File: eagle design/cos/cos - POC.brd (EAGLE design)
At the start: 35 x 63 mm, 97 parts, among them IC1 TPS630702RNMT, IC10 LM74670QDGKRQ1, IC11 SQJ886EP-T1_GE3, IC13 LDK320M50R, IC14 MCP2515, IC15 LM74670QDGKRQ1, IC16 MCP2561-2, IC17 AD5160BRJZ5-R2, IC18 MP3221GJ-P, IC2 LM74670QDGKRQ1, IC3 LMP92064SD/NOPB, IC4 SQJ960EP-T1_GE3, IC5 ATTINY4313-MMH, IC6 LM74670QDGKRQ1, IC7 PBRC8.00GR50X000, IC8 LM74670QDGKRQ1, IC9 SQJ960EP-T1_GE3, J1 22-27-2021-02

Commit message: - added MCP23S08 - 8-Bit IO Expander with Serial Interface
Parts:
- removed JP4: (no value), jumper:JP1
- added C35: 22μF, rcl:C0402
- added IC19: MP3221GJ-P, MP3221–2.7A, 1.2MHZ, HIGH-EFFICIENCY STEP UP CONVERTER WITH INPUT DISCONNECT:TSOT23-6
- added R23: 120, rcl:R0402
- added TP8: PTR1TP10SQ, testpad:TP10SQ
- C27: value 1μF -> 0.1μF
- C29: value 4.7μF -> 1μF
- C30: value 0.1μF -> 4.7μF
- C32: value 10μF -> 0.1μF
- C33: value 0.1μF -> 10μF
- C34: value 22μF -> 0.1μF
- IC15: value LM74670QDGKRQ1 -> MCP23S08-E/ML; device LM74670 - Smart Diode Rectifier Controller:VSSOP-8 -> MCP23S08 - 8-Bit IO Expander with Serial Interface:QFN20
- IC16: value MCP2561-2 -> LM74670QDGKRQ1; device MCP2561-2 - High-Speed CAN Transceiver:DFN10 -> LM74670 - Smart Diode Rectifier Controller:VSSOP-8
- IC17: value AD5160BRJZ5-R2 -> MCP2561-2; device ad5160 - 256-Position SPI-Compatible Digital Potentiometer:SOT-23-8 -> MCP2561-2 - High-Speed CAN Transceiver:DFN10
- IC18: value MP3221GJ-P -> AD5160BRJZ5-R2; device MP3221–2.7A, 1.2MHZ, HIGH-EFFICIENCY STEP UP CONVERTER WITH INPUT DISCONNECT:TSOT23-6 -> ad5160 - 256-Position SPI-Compatible Digital Potentiometer:SOT-23-8
- R12: value 741X083103JP / 10kΩ -> 1k; device 741X083331JP Resistor Array:0402 -> rcl:R0402
- R13: value 1k -> 270k
- R14: value 270k -> 741X083331JP / 330Ω; device rcl:R0402 -> 741X083331JP Resistor Array:0402
- R15: value thermistor NTC 10k -> 741X083103JP / 10kΩ; device rcl:V526-0 -> 741X083331JP Resistor Array:0402
- R16: value 741X083331JP / 330Ω -> 10k; device 741X083331JP Resistor Array:0402 -> rcl:R0402
- R17: value 22k -> thermistor NTC 10k; device rcl:R0402 -> rcl:V526-0
- R18: value 100k -> 22k
- R20: value 653k -> 100k
- R21: value 100k -> 653k
- R22: value 120 -> 100k
- TP6: value PTR1TP10SQ -> Li-Ion Cell +; device testpad:TP10SQ -> testpad:P1-13
- moved R16 183.8 mm to (3.00, -79.5), flipped to the top, turned to 0 degrees
- moved TP5 181.0 mm to (170.0, 18.0)
- moved C26 177.2 mm to (3.50, -74.5), flipped to the top, turned to 0 degrees
- moved JP1 109.9 mm to (101.5, 42.5), turned to 180 degrees
- moved R19 77.3 mm to (102.0, 48.2), turned to 0 degrees
- moved TP6 73.9 mm to (170.0, 20.5)
- moved R17 67.3 mm to (166.8, 31.2), turned to 0 degrees
- moved C30 63.6 mm to (169.8, 29.5), turned to 270 degrees
- moved C31 55.7 mm to (110.2, 52.0), turned to 180 degrees
- moved IC16 55.2 mm to (110.2, 52.0), flipped to the top
- moved IC15 55.0 mm to (162.0, 33.5), turned to 90 degrees
- moved C32 17.9 mm to (154.0, 17.5), turned to 90 degrees
- moved R15 16.1 mm to (154.5, 20.8), turned to 90 degrees
- moved IC17 15.3 mm to (151.2, 15.0), flipped to the bottom, turned to 270 degrees
- moved C29 14.7 mm to (159.8, 18.8), turned to 0 degrees
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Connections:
- net INT renamed INT_MCP2515
- removed net SPI_SS: IC14.!CS!, IC5.14, R16.7
- new net 5V9_LDO: IC15.4_!RESET!
- new net INT_MCP23S08: IC15.7_INT
- new net MCP23S08_GP0: IC15.9_GP0
- new net MCP23S08_GP1: IC15.10_GP1
- new net MCP23S08_GP2: IC15.11_GP2
- new net MCP23S08_GP3: IC15.12_GP3
- new net MCP23S08_GP4: IC15.13_GP4
- new net MCP23S08_GP5: IC15.14_GP5
- new net MCP23S08_GP6: IC15.15_GP6
- new net MCP23S08_GP7: IC15.16_GP7
- new net SPI_SS_MCP23S08: IC15.5_!CS!, R16.1
- new net SPI_SS_MCP2515: IC14.!CS!, IC5.14, R14.7
- net 5V0_LDO: now also C27.1, C29.2, C32.1, IC15.18_VCC, IC17.VDD, R14.8, R15.1, R15.3, R15.5, R15.7, R16.2; no longer C28.2, C31.1, IC16.VDD, R12.1, R12.3, R12.5, R12.7, R16.8
- net 5V0_TP-OUT: now also C34.1, IC18.2_VDD; no longer C33.1, IC17.2_VDD
- net 6V0: now also C28.1, C35.1, R21.2; no longer C27.1, C34.1, R20.2
- net AD5160_CS: now also IC18.6_!CS!, R15.8; no longer IC17.6_!CS!, R12.8
- net CANH: now also IC17.CANH, R23.2; no longer IC16.CANH, R22.2
- net CANL: now also IC17.CANL, R23.1; no longer IC16.CANL, R22.1
- net COMP_IN: now also R19.2; no longer R18.2
- net D4_GATE: now also IC16.GATE_DRIVE, IC16.GATE_PULLD; no longer IC15.GATE_DRIVE, IC15.GATE_PULLD
- net D4_VCAPH: now also C31.2, IC16.VCAPH; no longer C30.2, IC15.VCAPH
- net D4_VCAPL: now also C31.1, IC16.VCAPL; no longer C30.1, IC15.VCAPL
- net DELON_1: now also JP3.1; no longer JP4.1
- net DYNAMO2_C: now also JP2.2; no longer JP3.2
- net DYNAMO_2: now also IC16.CATHODE, JP1.1, JP3.2; no longer IC15.CATHODE, JP3.1, JP4.2
- net EN: now also IC19.4_EN, R20.1; no longer IC18.4_EN, R19.1
- net FB: now also IC19.3_FB, R21.1, R22.2; no longer IC18.3_FB, R20.1, R21.2
- net GND: now also C28.2, C30.1, C35.2, IC15.17_GND, IC15.2_A1, IC15.3_A0, IC15.GND, IC16.ANODE, IC17.GND, IC17.VSS, IC18.3_GND, IC18.7_B, IC19.2_GND, R13.1, R18.1, R22.1, TP5.TP; no longer C28.1, C31.2, IC15.ANODE, IC16.GND, IC16.VSS, IC17.3_GND, IC17.7_B, IC18.2_GND, R14.1, R15.1, R21.1
- net ICSP_DI/MISO: now also R14.5; no longer R16.5
- net ICSP_DO/MOSI: now also R14.3; no longer R16.3
- net ICSP_SCK: now also R14.1; no longer R16.1
- net LMP92064SD_CS: now also R15.6; no longer R12.6
- net N$2: now also JP1.2; no longer JP2.2
- net N$4: now also R18.2, R19.1; no longer R17.2, R18.1
- net N$8: now also R12.2, R17.2; no longer R14.2, R15.2
- net PROG1: now also IC18.1_W; no longer IC17.1_W
- net RESET: now also R15.4; no longer R12.4
- net RXCAN: now also IC17.RXD; no longer IC16.RXD
- net SPI_MISO: now also IC15.20_MISO, R14.6; no longer R16.6
- net SPI_MOSI: now also IC15.1_MOSI, IC18.5_SDI, R14.4; no longer IC17.5_SDI, R16.4
- net SPI_SCK: now also IC15.19_SCK, IC18.4_CLK, R14.2; no longer IC17.4_CLK, R16.2
- net STBY: now also IC17.STBY, R15.2; no longer IC16.STBY, R12.2
- net SW: now also IC19.1_SW; no longer IC18.1_SW
- net THERM: now also R12.1; no longer R13.1
- net TXCAN: now also IC17.TXD; no longer IC16.TXD
- net V_LI-ION_BATTERY: now also TP6.TP; no longer TP5.TP
- net V_LI-ION_OUT: now also C30.2, C33.1, IC19.5_IN, R20.2; no longer C29.2, C32.1, IC18.5_IN, R19.2
- net V_REGULATED_TP-IN: now also TP7.TP; no longer TP6.TP
- net V_REGULATED_TP-OUT: now also TP8.TP; no longer TP7.TP
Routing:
- net SPI_SS_MCP2515: track 0.00 -> 11.4 mm, vias 0 -> 1
- net SPI_SS: track 11.4 -> 0.00 mm, vias 1 -> 0
- net V_LI-ION_BATTERY: track 4.74 -> 7.71 mm

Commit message: - added FDMQ8403 4x N-Channel quad FET for FET-based bridge rectifier - added SQJ952EP-T1_GE3 - Dual N-Fet for FET-based AC capacitor switch
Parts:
- added IC20, IC21, IC22: SQJ952EP-T1_GE3, SQJ952EP-T1_GE3 - Dual N-Fet:SO-8L
- added IC23: (no value), FDMQ8403 4x N-Channel Fet:MLP-12
- added R24, R25, R26: 10k, rcl:R0402
- moved R16 198.9 mm to (167.0, 33.0), turned to 180 degrees
- moved C26 189.0 mm to (157.0, 35.8)
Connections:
- removed net N$2: C5.-, JP1.2
- new net GATE_DELON: IC22.G1, IC22.G2, R24.2
- new net GATE_GRAETZ: IC21.G1, IC21.G2, R25.1
- new net GATE_TUNING-CAP: IC20.G1, IC20.G2, R26.2
- new net N$13: IC20.S1, IC20.S2
- new net N$16: IC21.S1, IC21.S2
- new net N$20: IC22.S1, IC22.S2
- new net TUNING_CAP_DRAIN: C5.-, IC20.D1_1, IC20.D1_2, IC20.D1_3, JP1.2
- net 5V0_LDO: now also R25.2
- net DELON_1: now also IC22.D1_1, IC22.D1_2, IC22.D1_3
- net DYNAMO2_C: now also IC21.D1_1, IC21.D1_2, IC21.D1_3
- net DYNAMO_2: now also IC20.D2_1, IC20.D2_2, IC20.D2_3, IC21.D2_1, IC21.D2_2, IC21.D2_3, IC22.D2_1, IC22.D2_2, IC22.D2_3
- net GND: now also R24.1, R26.1
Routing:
- net TUNING_CAP_DRAIN: track 0.00 -> 9.91 mm
- net N$2: track 9.91 -> 0.00 mm
- net N$20: track 0.00 -> 4.44 mm
- net N$16: track 0.00 -> 4.44 mm
- net N$13: track 0.00 -> 4.44 mm
- net GATE_TUNING-CAP: track 0.00 -> 4.14 mm
- net GATE_GRAETZ: track 0.00 -> 4.14 mm
- net GATE_DELON: track 0.00 -> 4.14 mm

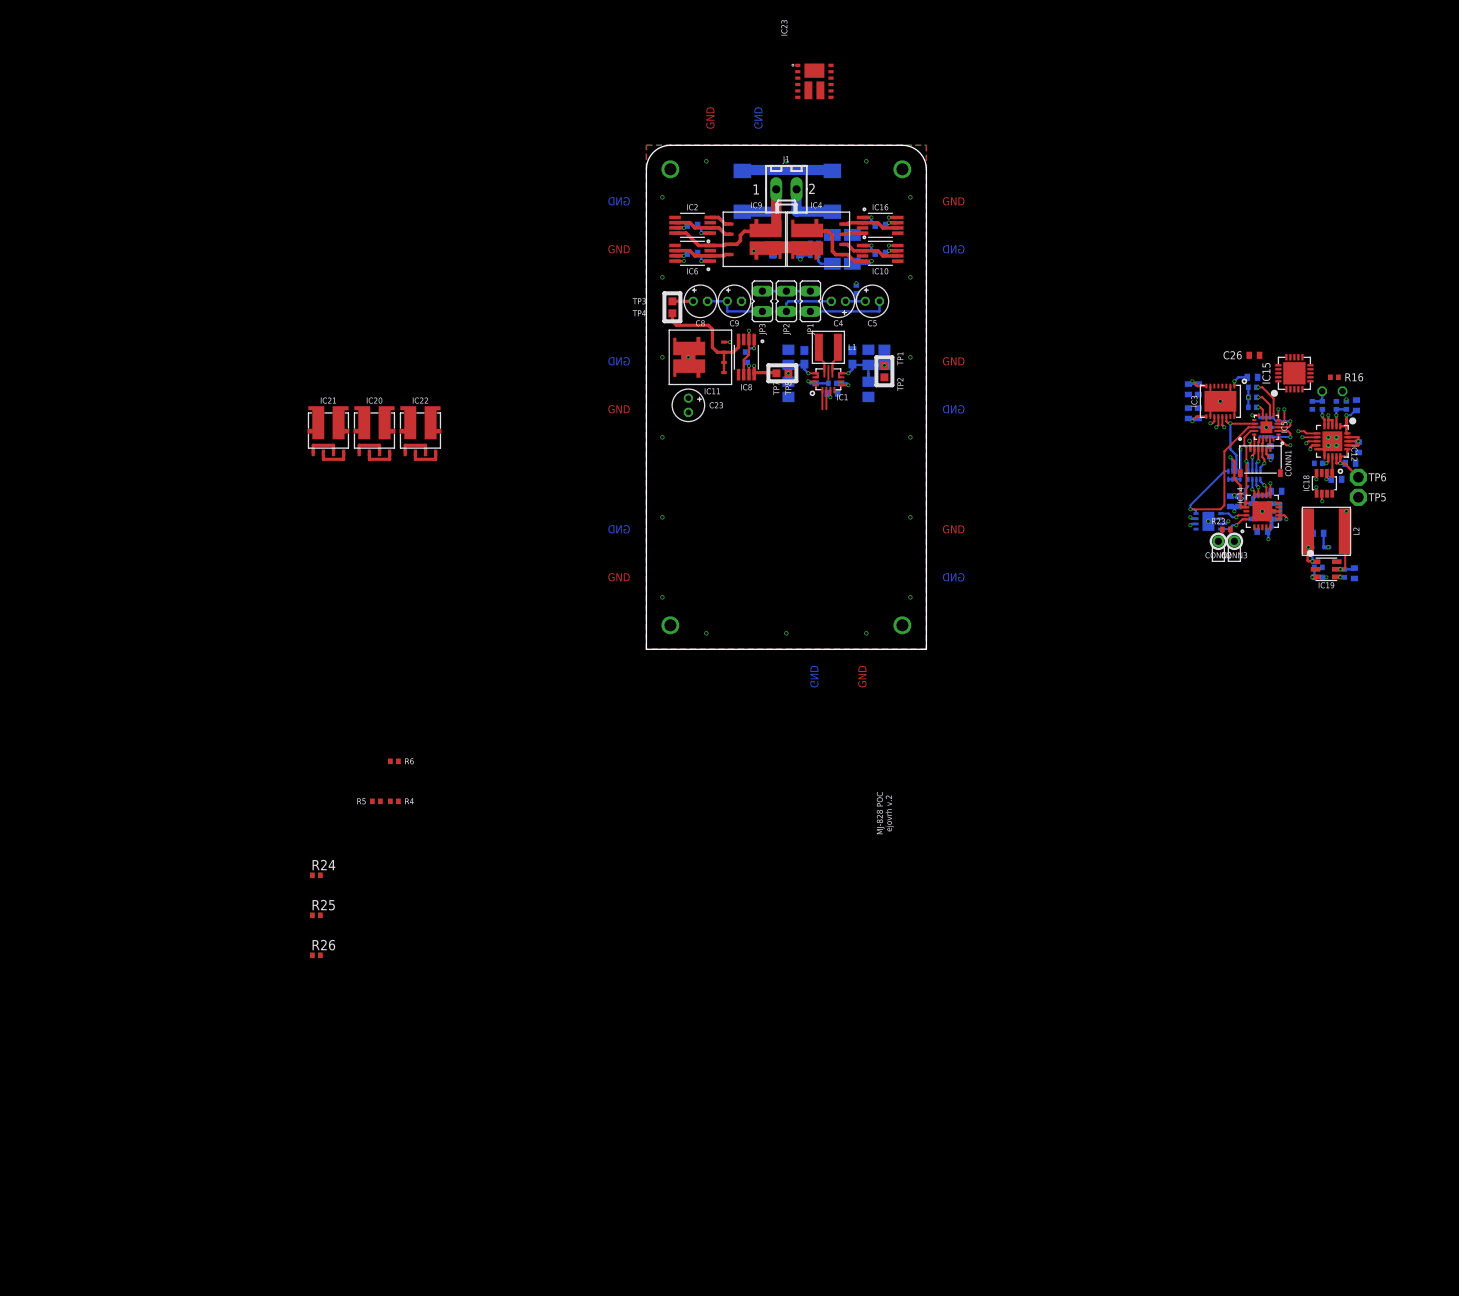
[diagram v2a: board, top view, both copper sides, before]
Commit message: - work on cos: replaced 2 fet bridge with one quad fet: FDMQ8403 4x N-Channel Fet
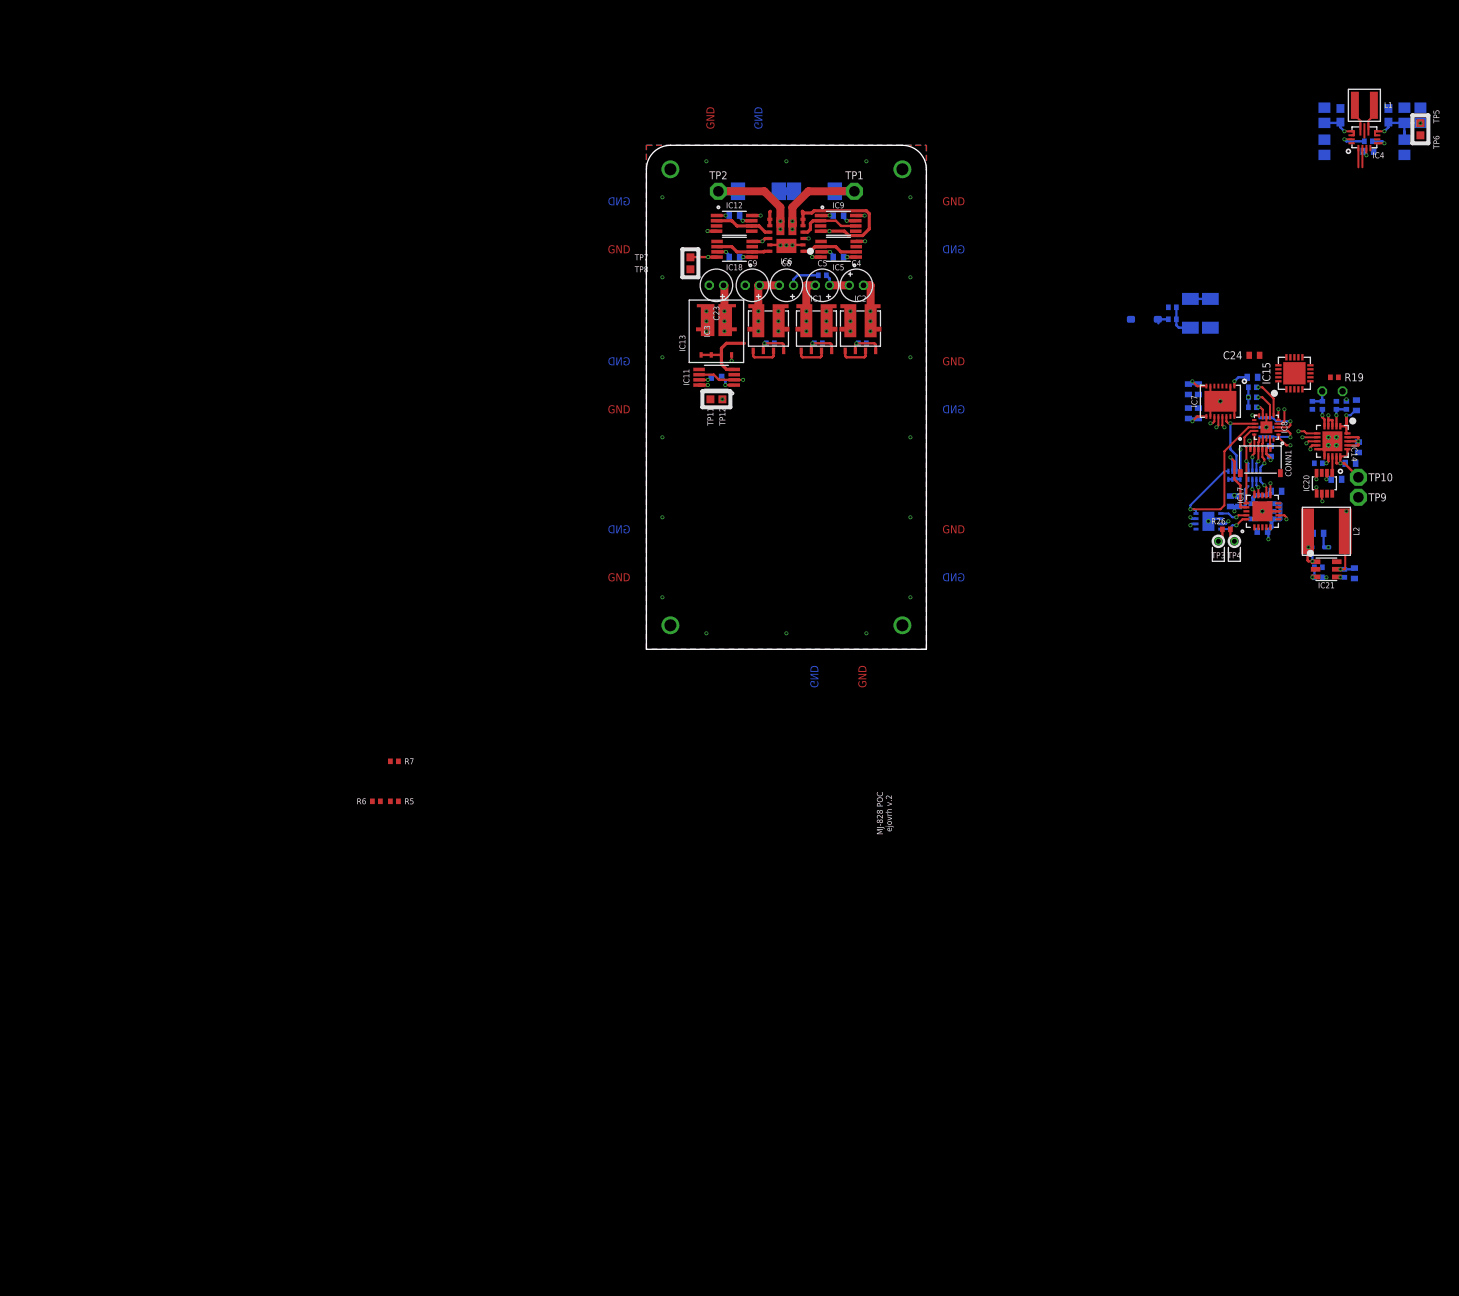
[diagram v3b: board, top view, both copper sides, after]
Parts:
- removed CONN2: CAN Low, signal testpoint:TH-0.9MM
- removed CONN3: CAN High, signal testpoint:TH-0.9MM
- removed IC22: SQJ952EP-T1_GE3, SQJ952EP-T1_GE3 - Dual N-Fet:SO-8L
- removed IC23: (no value), FDMQ8403 4x N-Channel Fet:MLP-12
- removed J1: 22-27-2021-02, con-molex:6410-02
- removed JP1, JP2, JP3: (no value), jumper:JP1
- added TP10, TP9: Li-Ion Cell +, testpad:P1-13
- added TP11, TP12: PTR1TP10SQ, testpad:TP10SQ
- C12: value 10μF -> 1μF; device rcl:C0805 -> rcl:C0402
- C14: value 1μF -> 10pF
- C18: value 10pF -> 10μF; device rcl:C0402 -> rcl:C0805
- C24: value 10μF -> 0.1μF
- C25: value 0.1μF -> 10μF
- IC1: value TPS630702RNMT -> SQJ952EP-T1_GE3; device TPS630701 - Buck Boost 5V regulator:VQFN -> SQJ952EP-T1_GE3 - Dual N-Fet:SO-8L
- IC10: value LM74670QDGKRQ1 -> PBRC8.00GR50X000; device LM74670 - Smart Diode Rectifier Controller:VSSOP-8 -> PRQV8.00CR1510Y00L - 8MHz resonator:SMT
- IC11: value SQJ886EP-T1_GE3 -> LM74670QDGKRQ1; device SQJ886EP - N-FET:SO-8L -> LM74670 - Smart Diode Rectifier Controller:VSSOP-8
- IC12: value (none) -> LM74670QDGKRQ1; device MCP73871 - Powerpath and Charge Controller:QFN50P400X400X100-21N -> LM74670 - Smart Diode Rectifier Controller:VSSOP-8
- IC13: value LDK320M50R -> SQJ886EP-T1_GE3; device LDK320 5V LDO:SOT-23-5L -> SQJ886EP - N-FET:SO-8L
- IC14: value MCP2515 -> (none); device MCP2515-I-ML - Standalonce CAN Controller with SPI Interface:QFN20 -> MCP73871 - Powerpath and Charge Controller:QFN50P400X400X100-21N
- IC16: value LM74670QDGKRQ1 -> LDK320M50R; device LM74670 - Smart Diode Rectifier Controller:VSSOP-8 -> LDK320 5V LDO:SOT-23-5L
- IC17: value MCP2561-2 -> MCP2515; device MCP2561-2 - High-Speed CAN Transceiver:DFN10 -> MCP2515-I-ML - Standalonce CAN Controller with SPI Interface:QFN20
- IC18: value AD5160BRJZ5-R2 -> LM74670QDGKRQ1; device ad5160 - 256-Position SPI-Compatible Digital Potentiometer:SOT-23-8 -> LM74670 - Smart Diode Rectifier Controller:VSSOP-8
- IC19: value MP3221GJ-P -> MCP2561-2; device MP3221–2.7A, 1.2MHZ, HIGH-EFFICIENCY STEP UP CONVERTER WITH INPUT DISCONNECT:TSOT23-6 -> MCP2561-2 - High-Speed CAN Transceiver:DFN10
- IC2: value LM74670QDGKRQ1 -> SQJ952EP-T1_GE3; device LM74670 - Smart Diode Rectifier Controller:VSSOP-8 -> SQJ952EP-T1_GE3 - Dual N-Fet:SO-8L
- IC20: value SQJ952EP-T1_GE3 -> AD5160BRJZ5-R2; device SQJ952EP-T1_GE3 - Dual N-Fet:SO-8L -> ad5160 - 256-Position SPI-Compatible Digital Potentiometer:SOT-23-8
- IC21: value SQJ952EP-T1_GE3 -> MP3221GJ-P; device SQJ952EP-T1_GE3 - Dual N-Fet:SO-8L -> MP3221–2.7A, 1.2MHZ, HIGH-EFFICIENCY STEP UP CONVERTER WITH INPUT DISCONNECT:TSOT23-6
- IC3: value LMP92064SD/NOPB -> SQJ952EP-T1_GE3; device LMP92064SD - LMP92064 Precision Low-Side, 125-kSps Simultaneous Sampling Current Sensor and Voltage Monitor With SPI:WS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 -> SQJ952EP-T1_GE3 - Dual N-Fet:SO-8L
- IC4: value SQJ960EP-T1_GE3 -> TPS630702RNMT; device SQJ960EP - dual N-FET:SO-8L -> TPS630701 - Buck Boost 5V regulator:VQFN
- IC5: value ATTINY4313-MMH -> LM74670QDGKRQ1; device ATtiny4313 microcontroller:VQFN-20 -> LM74670 - Smart Diode Rectifier Controller:VSSOP-8
- IC6: value LM74670QDGKRQ1 -> FDMQ8403; device LM74670 - Smart Diode Rectifier Controller:VSSOP-8 -> FDMQ8403 4x N-Channel Fet:MLP-12
- IC7: value PBRC8.00GR50X000 -> LMP92064SD/NOPB; device PRQV8.00CR1510Y00L - 8MHz resonator:SMT -> LMP92064SD - LMP92064 Precision Low-Side, 125-kSps Simultaneous Sampling Current Sensor and Voltage Monitor With SPI:WS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
- IC8: value LM74670QDGKRQ1 -> ATTINY4313-MMH; device LM74670 - Smart Diode Rectifier Controller:VSSOP-8 -> ATtiny4313 microcontroller:VQFN-20
- IC9: value SQJ960EP-T1_GE3 -> LM74670QDGKRQ1; device SQJ960EP - dual N-FET:SO-8L -> LM74670 - Smart Diode Rectifier Controller:VSSOP-8
- R1: value 47k -> 10k
- R10: value 10k -> 47k
- R11, R4: value 100k -> 47k
- R12: value 1k -> 47k
- R13: value 270k -> 10k
- R14: value 741X083331JP / 330Ω -> 100k; device 741X083331JP Resistor Array:0402 -> rcl:R0402
- R15: value 741X083103JP / 10kΩ -> 1k; device 741X083331JP Resistor Array:0402 -> rcl:R0402
- R16: value 10k -> 270k
- R17: value thermistor NTC 10k -> 741X083331JP / 330Ω; device rcl:V526-0 -> 741X083331JP Resistor Array:0402
- R18: value 22k -> 741X083103JP / 10kΩ; device rcl:R0402 -> 741X083331JP Resistor Array:0402
- R19: value 100k -> 10k
- R2: value 337k -> 10k
- R20: value 100k -> thermistor NTC 10k; device rcl:R0402 -> rcl:V526-0
- R21: value 653k -> 22k
- R23: value 120 -> 100k
- R24: value 10k -> 653k
- R25: value 10k -> 100k
- R26: value 10k -> 120
- R3: value 110k -> 10k
- R7: value 47k -> 100k
- R8: value 47k -> 337k
- R9: value 47k -> 110k
- TP1, TP2: value PTR1TP10SQ -> Li-Ion Cell +; device testpad:TP10SQ -> testpad:P1-13
- TP3: value PTR1TP10SQ -> CAN Low; device testpad:TP10SQ -> signal testpoint:TH
- TP4: value PTR1TP10SQ -> CAN High; device testpad:TP10SQ -> signal testpoint:TH
- TP5, TP6: value Li-Ion Cell + -> PTR1TP10SQ; device testpad:P1-13 -> testpad:TP10SQ
- moved R25 132.6 mm to (165.0, 9.25), flipped to the bottom
- moved R24 130.7 mm to (165.0, 8.00), flipped to the bottom, turned to 180 degrees
- moved IC21 126.0 mm to (166.0, 9.00), turned to 270 degrees
- moved R26 125.6 mm to (153.5, 14.0)
- moved IC20 119.0 mm to (165.8, 19.8), turned to 180 degrees
- moved R7 116.0 mm to (49.5, -15.0), flipped to the top
- moved R4 84.8 mm to (103.0, 45.8), flipped to the bottom
- moved IC12 79.6 mm to (92.0, 52.2)
- moved IC18 79.3 mm to (92.0, 49.0), turned to 90 degrees
- moved IC4 77.3 mm to (170.8, 63.0), turned to 90 degrees
- moved C13 77.0 mm to (177.8, 65.8), turned to 90 degrees
- moved TP4 75.8 mm to (154.5, 12.5), turned to 180 degrees
- moved TP3 74.6 mm to (152.5, 12.5), turned to 180 degrees
- moved C1 73.5 mm to (165.8, 61.8)
- moved C10 73.5 mm to (173.8, 65.8)
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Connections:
- removed net D1_GATE: IC2.GATE_DRIVE, IC2.GATE_PULLD, IC4.G1
- removed net D2_GATE: IC4.G2, IC6.GATE_DRIVE, IC6.GATE_PULLD
- removed net D3_GATE: IC10.GATE_DRIVE, IC10.GATE_PULLD, IC9.G1
- removed net D4_GATE: IC16.GATE_DRIVE, IC16.GATE_PULLD, IC9.G2
- removed net DYNAMO2_C: C4.-, IC21.D1_1, IC21.D1_2, IC21.D1_3, JP2.2
- new net GATE_D1: IC5.GATE_DRIVE, IC5.GATE_PULLD, IC6.1_G1
- new net GATE_D2: IC6.4_G2, IC9.GATE_DRIVE, IC9.GATE_PULLD
- new net GATE_D3: IC12.GATE_DRIVE, IC12.GATE_PULLD, IC6.9_G3
- new net GATE_D4: IC18.GATE_DRIVE, IC18.GATE_PULLD, IC6.12_G4
- net 5V0_LDO: now also C19.1, C24.1, IC16.OUT, IC19.VDD, IC8.18, R17.8, R18.1, R18.3, R18.5, R18.7, R19.2, R2.2; no longer C15.1, C26.1, IC13.OUT, IC14.VDD, IC5.18, R14.8, R15.1, R15.3, R15.5, R15.7, R16.2, R25.2
- net 5V0_TP-IN: now also C18.1, IC4.5-FB, IC4.7-VOUT, IC4.8-VOUT, IC4.VOUT, R13.2, TP5.TP; no longer C12.1, IC1.5-FB, IC1.7-VOUT, IC1.8-VOUT, IC1.VOUT, R10.2, TP1.TP
- net 5V0_TP-OUT: now also C14.1, C15.1, C25.1, IC14.17_CE, IC14.18_IN1, IC14.19_IN2, IC14.3_SEL, IC14.4_PROG2, IC14.9_!TE!, IC20.2_VDD, IC7.8_VDD, IC7.9_VDIG, R10.2, R11.2, R12.2, TP6.TP; no longer C18.1, C19.1, C24.1, IC12.17_CE, IC12.18_IN1, IC12.19_IN2, IC12.3_SEL, IC12.4_PROG2, IC12.9_!TE!, IC18.2_VDD, IC3.8_VDD, IC3.9_VDIG, R2.2, R7.2, R9.2, TP2.TP
- net 6V0: now also IC16.EN, IC16.IN, R24.2; no longer IC13.EN, IC13.IN, R21.2
- net AD5160_CS: now also IC20.6_!CS!, IC8.1, R18.8; no longer IC18.6_!CS!, IC5.1, R15.8
- net CANH: now also IC19.CANH, R26.2, TP4.TP$1; no longer CONN3.TP$1, IC17.CANH, R23.2
- net CANL: now also IC19.CANL, R26.1, TP3.TP$1; no longer CONN2.TP$1, IC17.CANL, R23.1
- net CLOCKOUT: now also IC17.OSC1, IC8.4; no longer IC14.OSC1, IC5.4
- net COMP_IN: now also IC8.10, R22.2; no longer IC5.10, R19.2
- net D1_VCAPH: now also IC5.VCAPH; no longer IC2.VCAPH
- net D1_VCAPL: now also IC5.VCAPL; no longer IC2.VCAPL
- net D2_VCAPH: now also IC9.VCAPH; no longer IC6.VCAPH
- net D2_VCAPL: now also IC9.VCAPL; no longer IC6.VCAPL
- net D3_VCAPH: now also C26.2, IC12.VCAPH; no longer C25.2, IC10.VCAPH
- net D3_VCAPL: now also C26.1, IC12.VCAPL; no longer C25.1, IC10.VCAPL
- net D4_VCAPH: now also IC18.VCAPH; no longer IC16.VCAPH
- net D4_VCAPL: now also IC18.VCAPL; no longer IC16.VCAPL
- net D5_VCAPH: now also IC11.VCAPH; no longer IC8.VCAPH
- net D5_VCAPL: now also IC11.VCAPL; no longer IC8.VCAPL
- net DEBUGWIRE/RESET: now also IC8.19; no longer IC5.19
- net DELON_1: now also IC3.D1_1, IC3.D1_2, IC3.D1_3; no longer IC22.D1_1, IC22.D1_2, IC22.D1_3, JP3.1
- net DYNAMO_1: now also IC12.CATHODE, IC18.ANODE, IC6.10_D3/S4, IC6.D3/S4, TP2.TP; no longer IC2.CATHODE, IC4.D1, IC4.S2, IC6.ANODE, J1.1
- net DYNAMO_2: now also IC1.D2_1, IC1.D2_2, IC1.D2_3, IC2.D1_1, IC2.D1_2, IC2.D1_3, IC3.D2_1, IC3.D2_2, IC3.D2_3; no longer IC10.ANODE, IC16.CATHODE, IC20.D2_1, IC20.D2_2, IC20.D2_3, IC21.D2_1, IC21.D2_2, IC21.D2_3, IC22.D2_1, IC22.D2_2, IC22.D2_3, IC9.D2, IC9.S1, JP1.1, JP2.1, JP3.2
- net DYNAMO_2_C: now also C4.-, IC2.D2_1, IC2.D2_2, IC2.D2_3, IC5.ANODE, IC6.3_S1/D2, IC6.S1/D2, IC9.CATHODE, TP1.TP; no longer J1.2
- net EN: now also IC21.4_EN, IC4.14-EN, R13.1, R23.1; no longer IC1.14-EN, IC19.4_EN, R10.1, R20.1
- net FB: now also IC21.3_FB, R24.1, R25.2; no longer IC19.3_FB, R21.1, R22.2
- net GATE_DELON: now also IC3.G1, IC3.G2, R3.2; no longer IC22.G1, IC22.G2, R24.2
- net GATE_GRAETZ: now also IC2.G1, IC2.G2, R2.1; no longer IC21.G1, IC21.G2, R25.1
- net GATE_TUNING-CAP: now also IC1.G1, IC1.G2, R1.2; no longer IC20.G1, IC20.G2, R26.2
- net GND: now also C25.2, IC10.GND, IC12.ANODE, IC14.10_GND1, IC14.11_GND2, IC14.GND2, IC14.GND3, IC14.GND4, IC14.GND5, IC16.GND, IC17.GND6, IC19.GND, IC19.VSS, IC20.3_GND, IC20.7_B, IC21.2_GND, IC4.10-PGND, IC4.15-VSEL, IC4.4-GND, IC4.6-FB2, IC6.5_S2, IC6.6_S2, IC6.7_S3, IC6.8_S3, IC7.10_DGND, IC7.16_RESET, IC7.2_REFG, IC7.7_GND, IC7.GND1, IC8.11, IC8.8, IC8.GND, IC9.ANODE, R1.1, R14.1, R16.1, R20.1, R21.1, R25.1, R9.1, TP9.TP; no longer C26.2, IC1.10-PGND, IC1.15-VSEL, IC1.4-GND, IC1.6-FB2, IC12.10_GND1, IC12.11_GND2, IC12.GND2, IC12.GND3, IC12.GND4, IC12.GND5, IC12.GND6, IC13.GND, IC14.GND, IC16.ANODE, IC17.VSS, IC18.3_GND, IC18.7_B, IC19.2_GND, IC2.ANODE, IC3.10_DGND, IC3.16_RESET, IC3.2_REFG, IC3.7_GND, IC3.GND1, IC4.S1, IC5.11, IC5.8, IC5.GND, IC7.GND, IC9.S2, R11.1, R13.1, R17.1, R18.1, R22.1, R24.1, R26.1, TP5.TP
- net ICSP_DI/MISO: now also IC8.15, R17.5; no longer IC5.15, R14.5
- net ICSP_DO/MOSI: now also IC8.16, R17.3; no longer IC5.16, R14.3
- net ICSP_SCK: now also IC8.17, R17.1; no longer IC5.17, R14.1
- net IDEAL_DIODE_GATE: now also IC11.GATE_DRIVE, IC11.GATE_PULLD, IC13.G; no longer IC11.G, IC8.GATE_DRIVE, IC8.GATE_PULLD
- net INT_MCP2515: now also IC17.!INT!, IC8.5; no longer IC14.!INT!, IC5.5
- net LMP92064SD_CS: now also IC7.14_CSB, IC8.12, R18.6; no longer IC3.14_CSB, IC5.12, R15.6
- net MCP73871_PG_PIN: now also IC14.!6_PG!, IC8.9, R10.1; no longer IC12.!6_PG!, IC5.9, R7.1
- net MCP73871_STAT1/!LBO!_PIN: now also IC14.8_STAT1/!LBO!, IC8.6, R11.1; no longer IC12.8_STAT1/!LBO!, IC5.6, R8.1
- net MCP73871_STAT2_PIN: now also IC14.7_STAT2, IC8.7, R12.1; no longer IC12.7_STAT2, IC5.7, R9.1
- net N$1: now also IC4.11-L1; no longer IC1.11-L1
- net N$10: now also IC7.4_INCN; no longer IC3.4_INCN
- net N$11: now also IC7.3_INCP; no longer IC3.3_INCP
- net N$12: now also IC7.6_INVG; no longer IC3.6_INVG
- net N$13: now also IC1.S1, IC1.S2; no longer IC20.S1, IC20.S2
- net N$14: now also R5.1, R6.2; no longer R4.1, R5.2
- net N$15: now also IC7.5_INVP; no longer IC3.5_INVP
- net N$16: now also IC2.S1, IC2.S2; no longer IC21.S1, IC21.S2
- net N$17: now also C12.1, IC7.1_REFC; no longer C14.1, IC3.1_REFC
- net N$20: now also IC3.S1, IC3.S2; no longer IC22.S1, IC22.S2
- net N$4: now also R21.2, R22.1; no longer R18.2, R19.1
- net N$5: now also IC4.9-L2; no longer IC1.9-L2
- net N$7: now also IC8.20; no longer IC5.20
- net N$8: now also R15.2, R16.2, R20.2; no longer R12.2, R13.2, R17.2
- net PG: now also IC4.2-PG; no longer IC1.2-PG
- net PROG1: now also IC14.13_PROG1, IC20.1_W; no longer IC12.13_PROG1, IC18.1_W
- net PROG3: now also IC14.12_PROG3, R14.2; no longer IC12.12_PROG3, R11.2
- net PS/SYNC: now also IC4.1-PS/S; no longer IC1.1-PS/S
- net RESET: now also IC17.!RESET!, R18.4; no longer IC14.!RESET!, R15.4
- net RXCAN: now also IC17.RXCAN, IC19.RXD; no longer IC14.RXCAN, IC17.RXD
- net SPI_MISO: now also IC17.SO, IC7.11_SDO, R17.6; no longer IC14.SO, IC3.11_SDO, R14.6
- net SPI_MOSI: now also IC17.SI, IC20.5_SDI, IC7.12_SDI, R17.4; no longer IC14.SI, IC18.5_SDI, IC3.12_SDI, R14.4
- net SPI_SCK: now also IC17.SCK, IC20.4_CLK, IC7.13_SCLK, R17.2; no longer IC14.SCK, IC18.4_CLK, IC3.13_SCLK, R14.2
- net SPI_SS_MCP23S08: now also R19.1; no longer R16.1
- net SPI_SS_MCP2515: now also IC17.!CS!, IC8.14, R17.7; no longer IC14.!CS!, IC5.14, R14.7
- net STBY: now also IC19.STBY, IC8.13, R18.2; no longer IC17.STBY, IC5.13, R15.2
- net SW: now also IC21.1_SW; no longer IC19.1_SW
- net THERM: now also IC14.5_THERM, R15.1; no longer IC12.5_THERM, R12.1
- net TUNING_CAP_DRAIN: now also IC1.D1_1, IC1.D1_2, IC1.D1_3; no longer IC20.D1_1, IC20.D1_2, IC20.D1_3, JP1.2
- net TUNIN_CAP2_BIAS: now also R4.1; no longer R1.1
- net TXCAN: now also IC17.TXCAN, IC19.TXD; no longer IC14.TXCAN, IC17.TXD
- net VAUX: now also IC4.3-VAUX; no longer IC1.3-VAUX
- net VPCC: now also IC14.2_VPCC, R8.1, R9.2; no longer IC12.2_VPCC, R2.1, R3.2
- net V_DC_TP-IN: now also IC18.CATHODE, IC5.CATHODE, IC6.11_D1/D4, IC6.2_D1/D4, IC6.D1/D4, R4.2, TP7.TP; no longer IC10.CATHODE, IC4.D2, IC6.CATHODE, IC9.D1, R1.2, TP3.TP
- net V_DC_TP-OUT: now also IC11.ANODE, IC13.S1, IC13.S2, IC13.S3, TP8.TP; no longer IC11.S1, IC11.S2, IC11.S3, IC8.ANODE, TP4.TP
- net V_LI-ION_BATTERY: now also IC14.14_VBAT1, IC14.15_VBAT2, IC14.16_BAT_SENSE, TP10.TP; no longer IC12.14_VBAT1, IC12.15_VBAT2, IC12.16_BAT_SENSE, TP6.TP
- net V_LI-ION_OUT: now also IC14.1_OUT1, IC14.20_OUT2, IC21.5_IN, R23.2; no longer IC12.1_OUT1, IC12.20_OUT2, IC19.5_IN, R20.2
- net V_REGULATED_TP-IN: now also IC11.CATHODE, IC13.D1, IC13.D2, TP11.TP; no longer IC11.D1, IC11.D2, IC8.CATHODE, TP7.TP
- net V_REGULATED_TP-OUT: now also IC4.12-VIN, IC4.13-VIN, IC4.VIN, TP12.TP; no longer IC1.12-VIN, IC1.13-VIN, IC1.VIN, TP8.TP
- net XTAL1: now also IC10.XTAL1, IC8.3; no longer IC5.3, IC7.XTAL1
- net XTAL2: now also IC10.XTAL2, IC8.2; no longer IC5.2, IC7.XTAL2
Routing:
- net DYNAMO_2_C: track 7.29 -> 40.9 mm, vias 0 -> 8
- net DYNAMO_2: track 38.7 -> 19.0 mm, vias 2 -> 9
- net COMP_IN: track 22.2 -> 2.71 mm, vias 2 -> 1
- net GND: track 25.6 -> 42.3 mm, vias 28 -> 30
- net V_DC_TP-IN: track 47.6 -> 31.1 mm, vias 4 -> 5
- net ZENER_COMMON: track 11.3 -> 1.90 mm
- net GATE_D2: track 0.00 -> 7.89 mm
- net D3_GATE: track 7.57 -> 0.00 mm
- net D1_GATE: track 7.57 -> 0.00 mm
- net D4_GATE: track 7.31 -> 0.00 mm
- net D2_GATE: track 7.31 -> 0.00 mm
- net GATE_D3: track 0.00 -> 7.24 mm
- net GATE_D1: track 0.00 -> 7.17 mm
- net GATE_D4: track 0.00 -> 6.89 mm
- net DYNAMO2_C: track 6.73 -> 0.00 mm
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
